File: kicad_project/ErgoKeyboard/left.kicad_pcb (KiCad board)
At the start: 2 copper layers, 163.8 x 116.3 mm, 51 parts

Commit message: added some components, tuning
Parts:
- added B1: , E73:SW_TACT_ALPS_SKQGABE010, F.Cu at (273.8, 155.7)
- added JST1: , JST_PH_S2B-PH-K_02x2.00mm_Angled, F.Cu at (272.3, 151.2)
- added OLED1: nice!view, lib:niceview, F.Cu at (273.0, 129.6)
- S1, S10, S11, S12, S13, S14, S15, S16, S17, S18, S19, S2, S20, S21, S22, S23, S24, S25, S3, S4, S5, S6, S7, S8, S9: value ks27-hs-reversible -> ks27; footprint lib:gateron-ks27-hotswap-reversible -> lib:gateron-ks27
- moved D17 230.5 mm to (229.8, 138.2)
- moved D18 230.5 mm to (231.2, 118.8)
- moved D19 230.5 mm to (232.5, 99.3)
- moved D22 230.5 mm to (254.2, 105.9)
- moved D23 230.5 mm to (249.9, 169.0)
- moved D5 230.5 mm to (169.1, 162.3)
- moved D8 230.5 mm to (167.0, 103.9)
- moved S17 230.5 mm to (229.1, 148.2)
- moved S18 230.5 mm to (230.5, 128.7)
- moved S19 230.5 mm to (231.8, 109.3)
- moved S20 230.5 mm to (248.2, 154.6)
- moved S23 230.5 mm to (245.4, 177.9)
- moved S24 230.5 mm to (264.9, 182.6)
- moved S7 230.5 mm to (168.1, 133.3)
- moved S8 230.5 mm to (167.4, 113.9)
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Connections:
- MCU1 pad 1: (no net) -> RAW
- MCU1 pad 10: (no net) -> P14
- MCU1 pad 11: (no net) -> P16
- MCU1 pad 12: (no net) -> P10
- MCU1 pad 13: (no net) -> P1
- MCU1 pad 14: (no net) -> P0
- MCU1 pad 15: (no net) -> GND
- MCU1 pad 16: (no net) -> GND
- MCU1 pad 17: (no net) -> P3
- MCU1 pad 18: (no net) -> P4
- MCU1 pad 19: (no net) -> P5
- MCU1 pad 2: (no net) -> GND
- MCU1 pad 20: (no net) -> P2
- MCU1 pad 21: (no net) -> P6
- MCU1 pad 22: (no net) -> P7
- MCU1 pad 23: (no net) -> P8
- MCU1 pad 24: (no net) -> P9
- MCU1 pad 3: (no net) -> RST
- MCU1 pad 4: (no net) -> VCC
- MCU1 pad 5: (no net) -> P21
- MCU1 pad 6: (no net) -> P20
- MCU1 pad 7: (no net) -> P19
- MCU1 pad 8: (no net) -> P18
- MCU1 pad 9: (no net) -> P15
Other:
- outline, holes or cut-outs redrawn

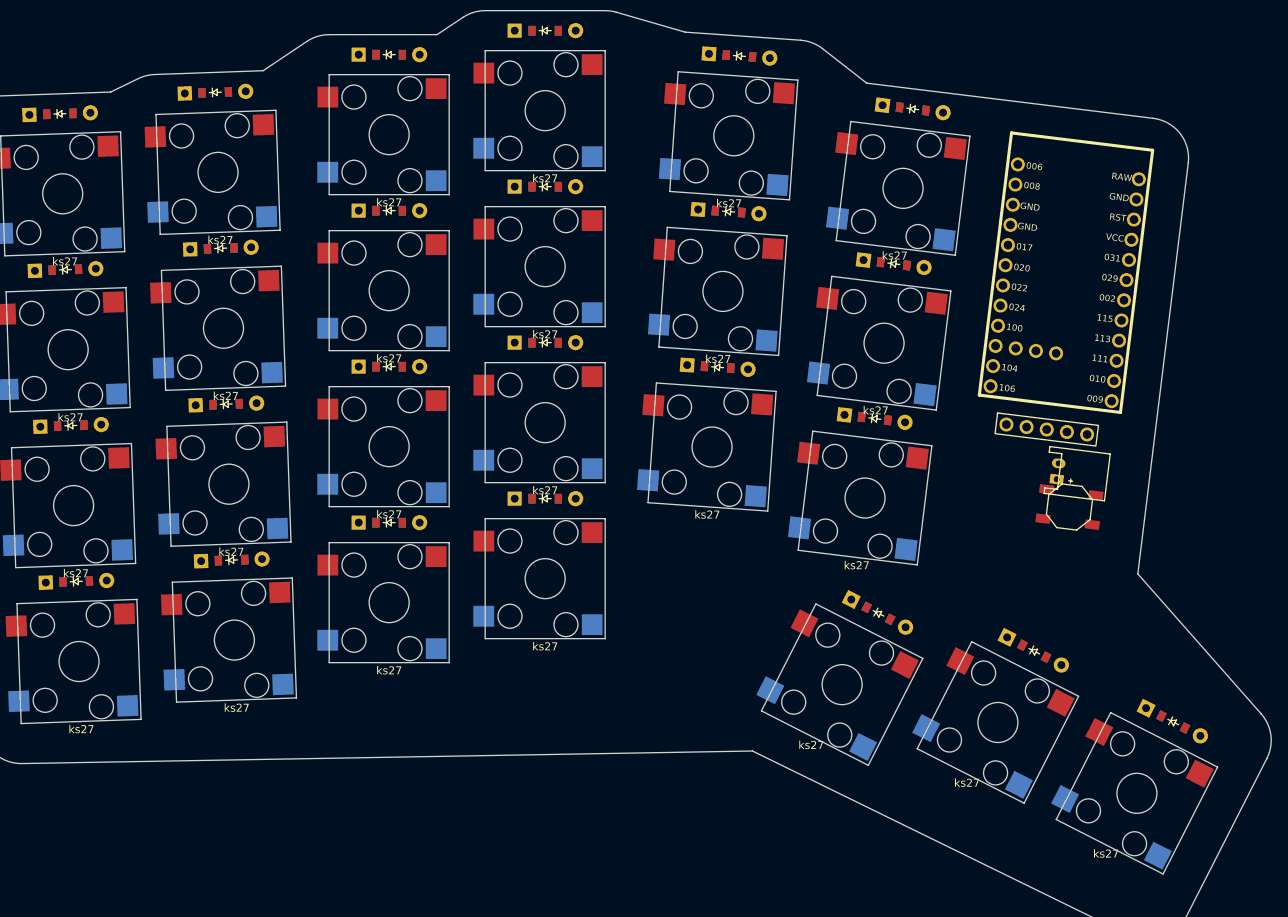
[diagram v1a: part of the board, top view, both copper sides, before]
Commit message: completed reversible micro fp, working on layout
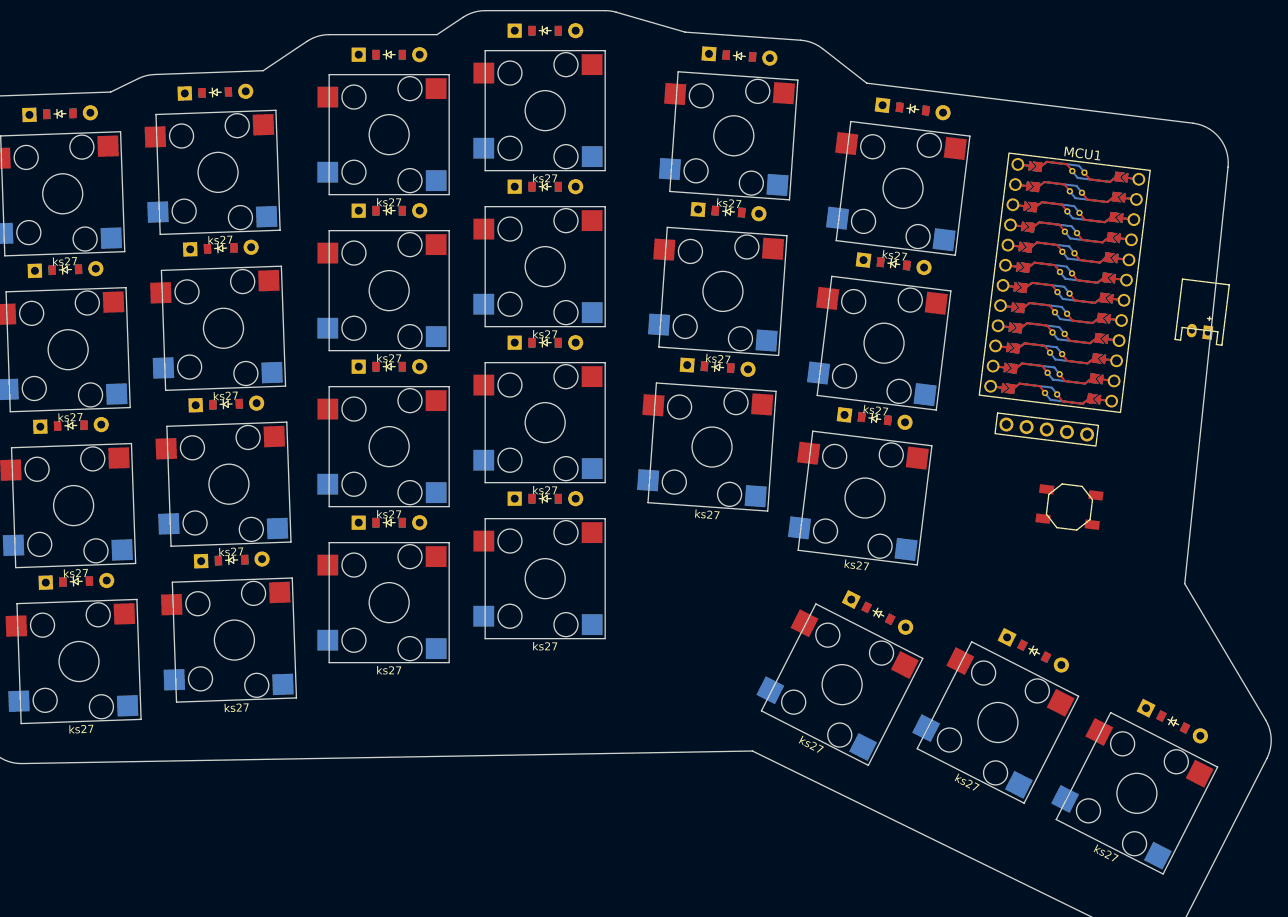
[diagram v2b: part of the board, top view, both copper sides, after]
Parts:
- MCU1: value nice_nano -> rev_mcu; footprint nicenano -> revmicro
- moved JST1 24.9 mm to (290.1, 133.8), turned to 173 degrees
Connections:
- MCU1 pad 1: RAW -> P1
- MCU1 pad 10: P14 -> P7
- MCU1 pad 11: P16 -> P8
- MCU1 pad 12: P10 -> P9
- MCU1 pad 13: P1 -> RAW
- MCU1 pad 14: P0 -> GND
- MCU1 pad 15: GND -> RST
- MCU1 pad 16: GND -> VCC
- MCU1 pad 17: P3 -> P21
- MCU1 pad 18: P4 -> P20
- MCU1 pad 19: P5 -> P19
- MCU1 pad 2: GND -> P0
- MCU1 pad 20: P2 -> P18
- MCU1 pad 21: P6 -> P15
- MCU1 pad 22: P7 -> P14
- MCU1 pad 23: P8 -> P16
- MCU1 pad 24: P9 -> P10
- MCU1 pad 3: RST -> GND
- MCU1 pad 4: VCC -> GND
- MCU1 pad 5: P21 -> P2
- MCU1 pad 6: P20 -> P3
- MCU1 pad 7: P19 -> P4
- MCU1 pad 8: P18 -> P5
- MCU1 pad 9: P15 -> P6
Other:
- outline, holes or cut-outs redrawn

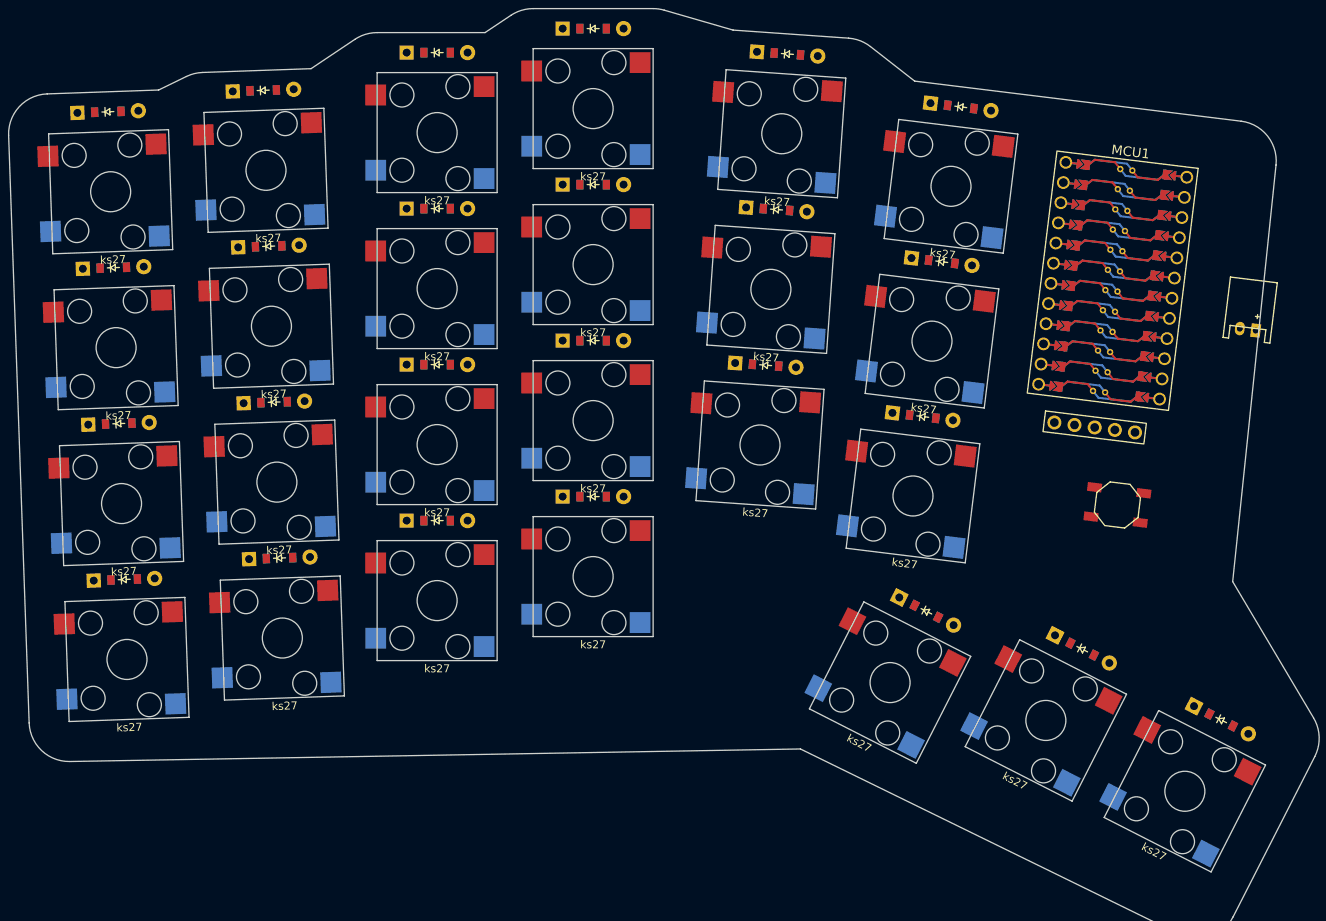
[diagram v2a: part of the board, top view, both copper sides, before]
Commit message: positioned jsth, need jumper fp for revers. oled
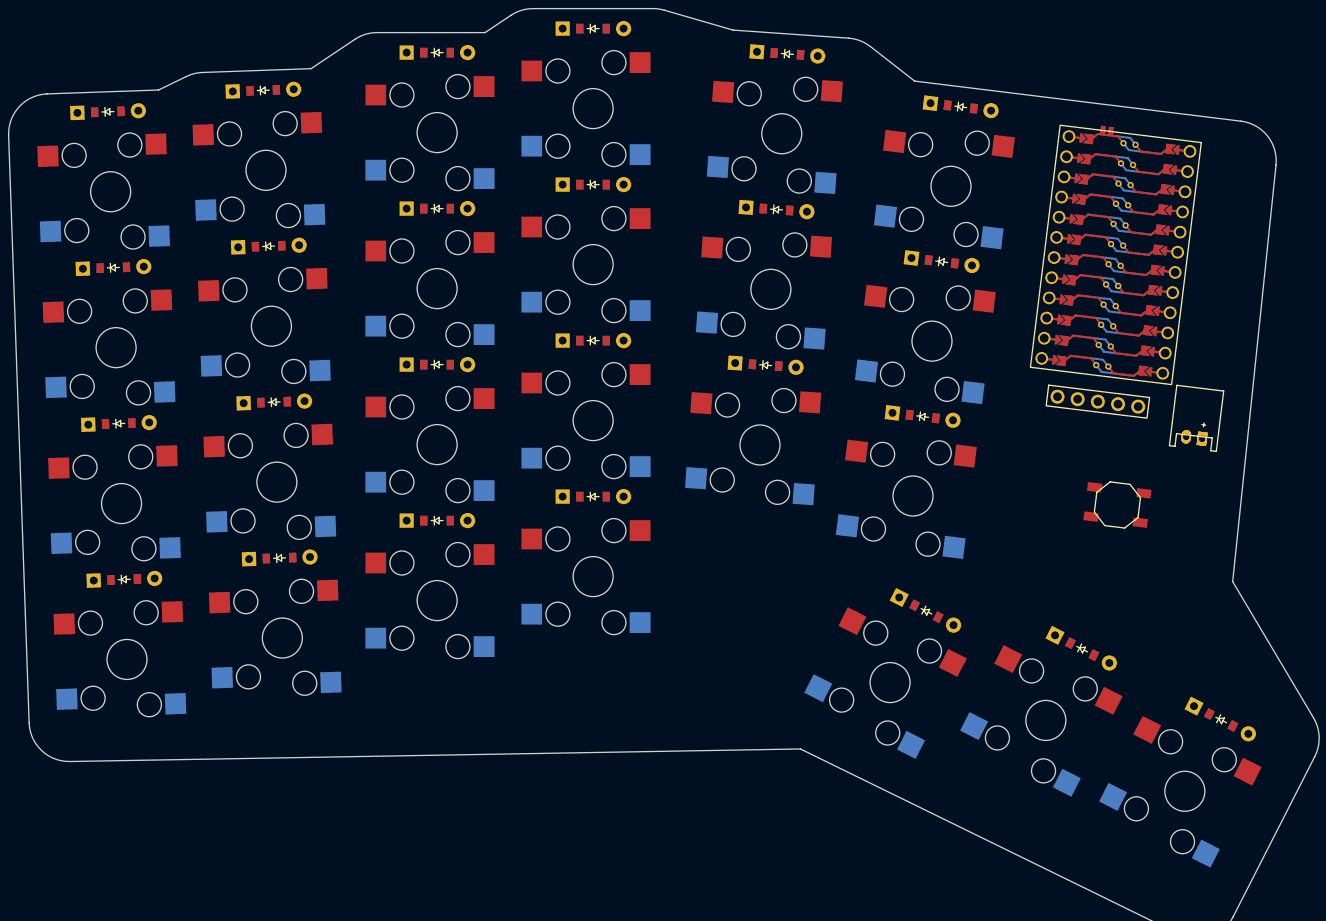
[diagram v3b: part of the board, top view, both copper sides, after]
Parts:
- added J1: Jumper, lib:Jumper, F.Cu at (272.5, 108.9)
- added JST2: , JST_PH_S2B-PH-K_02x2.00mm_Angled, F.Cu at (283.4, 147.3)
- moved JST1 15.1 mm to (283.4, 147.3)
- moved MCU1 3.25 mm to (273.6, 124.4)
- moved OLED1 3.25 mm to (273.4, 126.4)
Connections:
- MCU1 pad 13: RAW -> P10
- MCU1 pad 14: GND -> P16
- MCU1 pad 15: RST -> P14
- MCU1 pad 16: VCC -> P15
- MCU1 pad 17: P21 -> P18
- MCU1 pad 18: P20 -> P19
- MCU1 pad 19: P19 -> P20
- MCU1 pad 20: P18 -> P21
- MCU1 pad 21: P15 -> VCC
- MCU1 pad 22: P14 -> RST
- MCU1 pad 23: P16 -> GND
- MCU1 pad 24: P10 -> RAW
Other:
- outline, holes or cut-outs redrawn

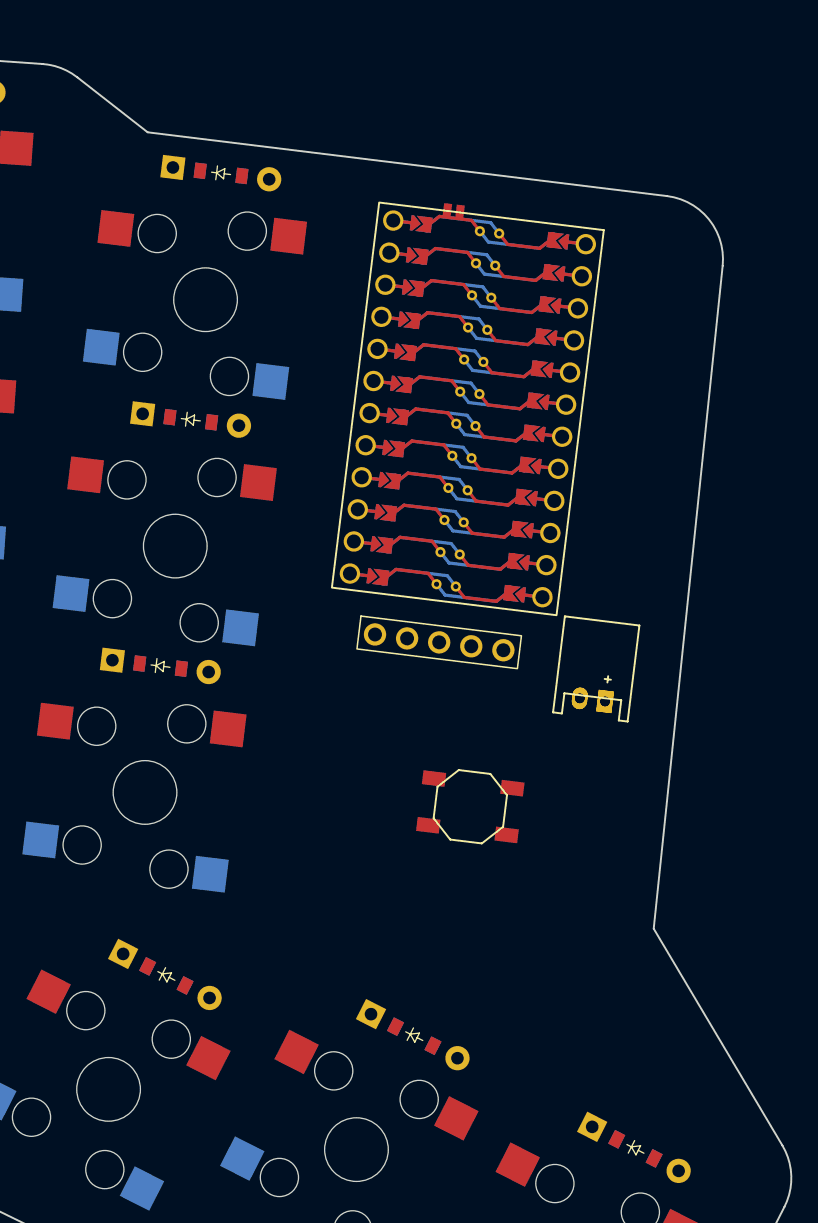
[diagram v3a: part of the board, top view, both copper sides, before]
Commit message: fixed most reversible stuff added footprints
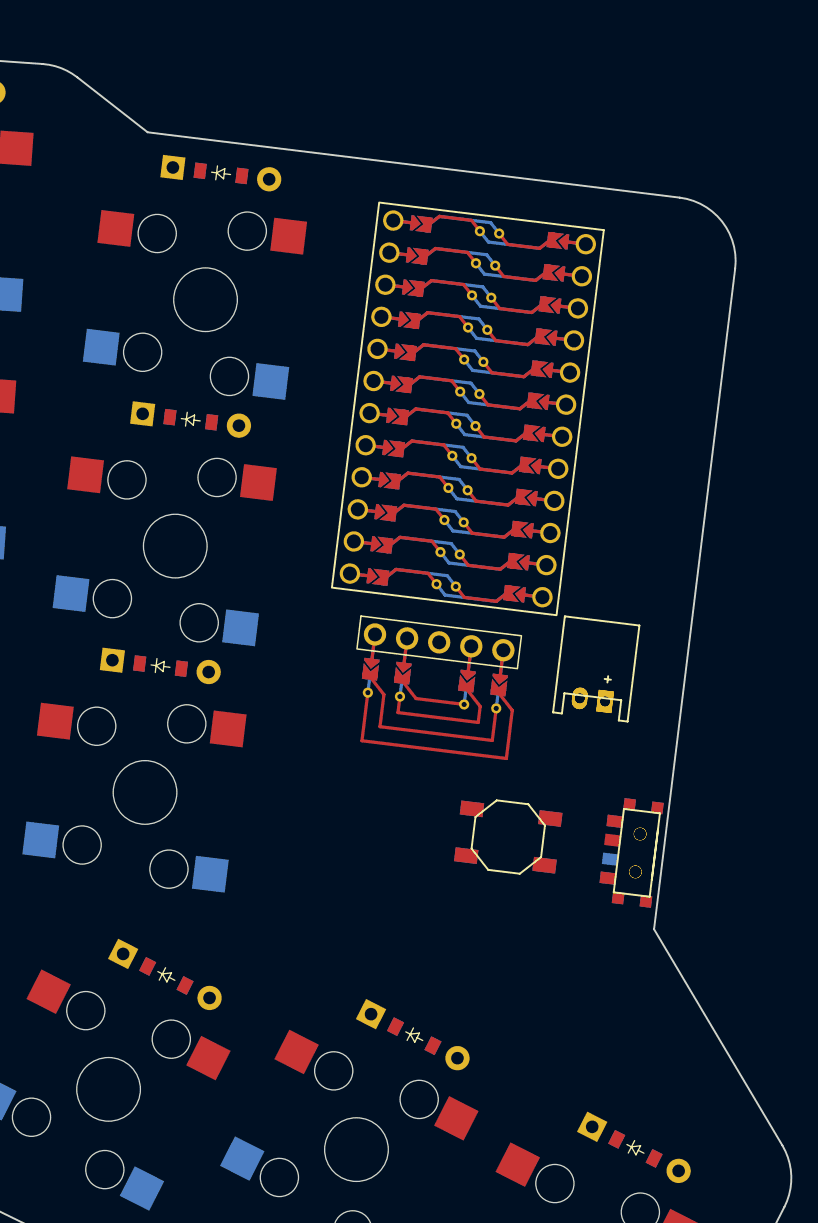
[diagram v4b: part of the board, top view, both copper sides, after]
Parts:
- removed J1: Jumper, lib:Jumper
- added B2: , E73:SW_TACT_ALPS_SKQGABE010, F.Cu at (276.8, 158.1)
- added T1, T2: , E73:SPDT_C128955, F.Cu at (287.0, 159.3)
- moved B1 3.82 mm to (276.8, 158.1)
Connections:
- JST1 pad 1: VCC -> BPOS
- JST2 pad 1: VCC -> BPOS
- OLED1 pad 1: P2 -> (no net)
- OLED1 pad 2: P3 -> (no net)
- OLED1 pad 4: GND -> (no net)
- OLED1 pad 5: P1 -> (no net)
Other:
- outline, holes or cut-outs redrawn

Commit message: starting the netting process
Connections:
- net home_default renamed home_cluster
- net inner_default renamed inner_cluster
- net outer_default renamed outer_cluster
- D1 pad 1: (no net) -> P9
- D10 pad 1: (no net) -> P8
- D11 pad 1: (no net) -> P7
- D12 pad 1: (no net) -> P6
- D13 pad 1: (no net) -> P9
- D14 pad 1: (no net) -> P8
- D15 pad 1: (no net) -> P7
- D16 pad 1: (no net) -> P6
- D17 pad 1: (no net) -> P8
- D18 pad 1: (no net) -> P7
- D19 pad 1: (no net) -> P6
- D2 pad 1: (no net) -> P8
- D20 pad 1: (no net) -> P8
- D21 pad 1: (no net) -> P7
- D22 pad 1: (no net) -> P6
- D23 pad 1: (no net) -> P9
- D24 pad 1: (no net) -> P9
- D25 pad 1: (no net) -> P9
- D3 pad 1: (no net) -> P7
- D4 pad 1: (no net) -> P6
- D5 pad 1: (no net) -> P9
- D6 pad 1: (no net) -> P8
- D7 pad 1: (no net) -> P7
- D8 pad 1: (no net) -> P6
- D9 pad 1: (no net) -> P9
- S1 pad 1: (no net) -> P10
- S10 pad 1: (no net) -> P14
- S11 pad 1: (no net) -> P14
- S12 pad 1: (no net) -> P14
- S13 pad 1: (no net) -> P15
- S14 pad 1: (no net) -> P15
- S15 pad 1: (no net) -> P15
- S16 pad 1: (no net) -> P15
- S17 pad 1: (no net) -> P18
- S18 pad 1: (no net) -> P18
- S19 pad 1: (no net) -> P18
- S2 pad 1: (no net) -> P10
- S20 pad 1: (no net) -> P19
- S21 pad 1: (no net) -> P19
- S22 pad 1: (no net) -> P19
- S23 pad 1: (no net) -> P18
- S24 pad 1: (no net) -> P19
- S25 pad 1: (no net) -> P19
- S3 pad 1: (no net) -> P10
- S4 pad 1: (no net) -> P10
- S5 pad 1: (no net) -> P16
- S6 pad 1: (no net) -> P16
- S7 pad 1: (no net) -> P16
- S8 pad 1: (no net) -> P16
- S9 pad 1: (no net) -> P14
